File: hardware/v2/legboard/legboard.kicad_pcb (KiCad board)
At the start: 2 copper layers, 40.6 x 45.7 mm, 17 parts, among them J1 UPLINK_RJ11, J2 COXA, J3 FEMUR, J4 TIBIA, J5 SERVO_PWR_IN, U1 XIAO-RP2040, U2 SP3485CN, U3 INA4181A3IPWR

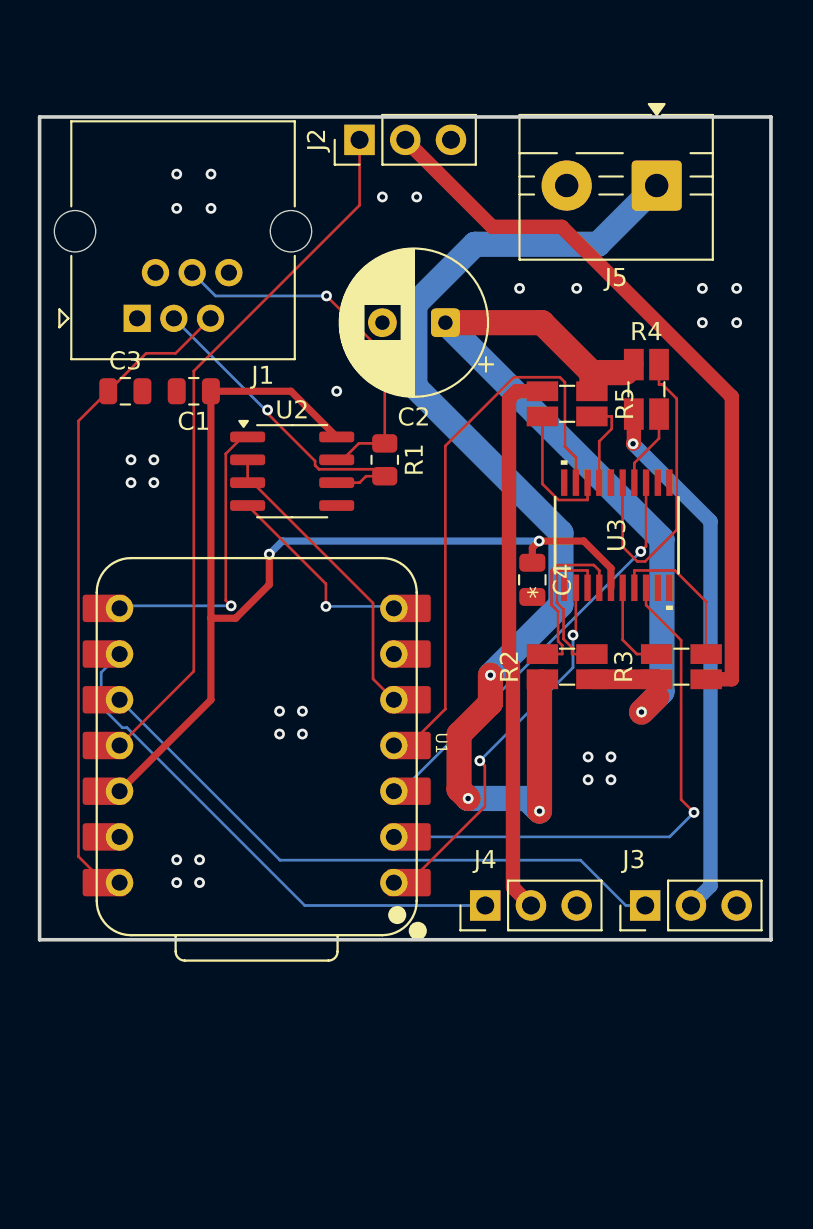
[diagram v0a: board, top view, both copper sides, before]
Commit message: legboard sensing corrections and shunt remapping
- Fix INA4181A3IPWR gain: was 3 (copy-paste error), correct value is 100
  per datasheet (A3 suffix = gain 100); V_TO_A scale was ~33x too high
- Remap shunt resistors for better PCB layout: R4=total, R5=coxa,
  R3=femur, R2=tibia (was R2=total, R3=coxa, R4=femur, R5=tibia)
- Update ADC pin assignments on XIAO to match new shunt layout:
  A0=total, A1=femur, A2=tibia, A3=coxa
- Add leg firmware test sketch (tibia servo sweep + current readout)
  targeting XIAO RP2040 via PlatformIO; kept for v2 board validation

Co-Authored-By: Claude Sonnet 4.6 <noreply@anthropic.com>
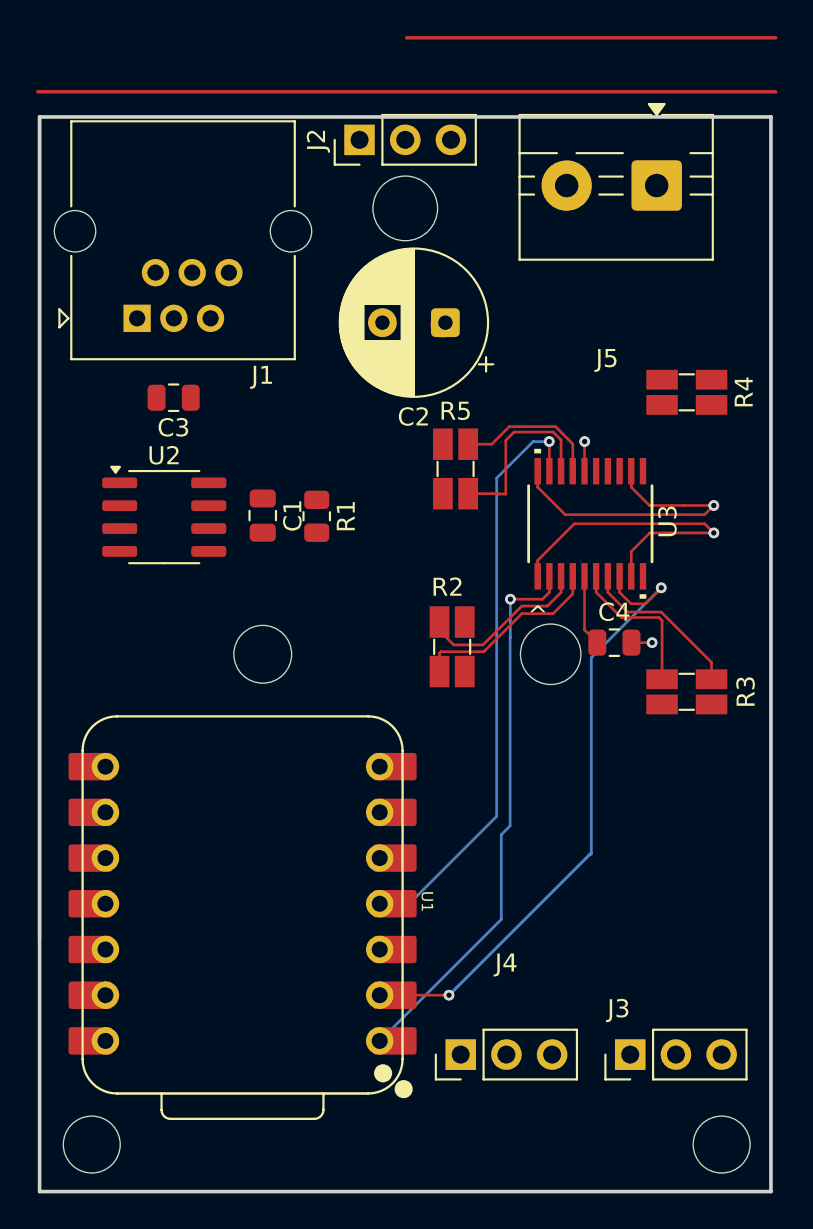
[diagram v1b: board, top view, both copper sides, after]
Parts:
- moved U1 8.83 mm to (112.9, 69.1)
- moved J4 8.40 mm to (125.0, 77.5)
- moved J3 8.33 mm to (134.4, 77.5)
- moved C1 7.90 mm to (114.0, 47.5), turned to -90 degrees
- moved U2 7.55 mm to (108.5, 47.6)
- moved R5 7.18 mm to (124.7, 45.0), turned to 0 degrees
- moved R2 6.48 mm to (124.5, 54.8), turned to 180 degrees
- moved C4 5.74 mm to (133.5, 54.6), turned to 0 degrees
- moved R1 4.91 mm to (117.0, 47.6)
- moved C3 2.71 mm to (109.0, 41.0), turned to 180 degrees
- moved R4 2.25 mm to (137.6, 40.7), turned to -90 degrees
- moved U3 1.60 mm to (132.2, 48.0)
- moved R3 1.43 mm to (137.6, 57.3)
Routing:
- net +6V_IN: track 61.2 -> 0.21 mm, vias 3 -> 0
- net +3.3V: track 61.3 -> 3.80 mm, vias 2 -> 0
- net +6V: track 45.7 -> 0.19 mm, vias 1 -> 0
- net +6V_COXA: track 41.2 -> 0.00 mm
- net COXA_PWM: track 40.0 -> 0.00 mm
- net GND: track 0.00 -> 38.5 mm, vias 29 -> 4
- net +5V: track 36.8 -> 0.00 mm
- net FEMUR_PWM: track 34.8 -> 0.00 mm
- net +6V_TIBIA: track 30.7 -> 0.00 mm
- net TIBIA_PWM: track 30.1 -> 0.00 mm
- net +6V_FEMUR: track 29.6 -> 0.00 mm, vias 1 -> 0
- net I_FEMUR_SENSE: track 24.0 -> 0.00 mm, vias 1 -> 0
- net RS485_B: track 20.6 -> 0.00 mm, vias 1 -> 0
- net RS485_A: track 19.4 -> 0.00 mm, vias 1 -> 0
- net RS485_DE: track 17.7 -> 0.00 mm
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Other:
- board size 40.6 x 45.7 mm -> 40.6 x 59.7 mm
